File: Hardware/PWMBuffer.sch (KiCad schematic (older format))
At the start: 3 parts, among them Q2 IRLZ44N

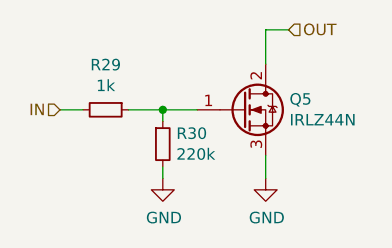
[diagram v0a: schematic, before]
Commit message: Board updates:
Fixed footprints (SMD vs. THT, no hanging pads in the air)
Added mounting holes for production
Moved F.Fab text to readable locations
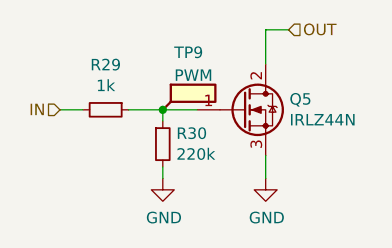
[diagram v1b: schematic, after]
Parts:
- added TP6: PWM, Measurement_Points:Measurement_Point_Round-SMD-Pad_Small, symbol Connector:TestPoint_Flag
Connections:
- net at Q2.1 (G), R23.1, R24.1: now also TP6.1
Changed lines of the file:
@@
 Wire Wire Line
 	2400 2500 2400 2550
+$Comp
+L Connector:TestPoint_Flag TP6
+U 1 1 5FA2C9EF
+P 2400 2250
+AR Path="/60041CA2/5FA2C9EF" Ref="TP6"  Part="1"
+AR Path="/60047352/5FA2C9EF" Ref="TP7"  Part="1"
+AR Path="/6005538F/5FA2C9EF" Ref="TP8"  Part="1"
+AR Path="/60055395/5FA2C9EF" Ref="TP9"  Part="1"
+F 0 "TP9" H 2450 2500 50  0000 L CNN
+F 1 "PWM" H 2450 2400 50  0000 L CNN
+F 2 "Measurement_Points:Measurement_Point_Round-SMD-Pad_Small" H 2600 2250 50  0001 C CNN
+F 3 "~" H 2600 2250 50  0001 C CNN
+	1    2400 2250
+	1    0    0    -1
+$EndComp
 $EndSCHEMATC

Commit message: Hardware v0.1, Firmware runs ADC trigger by TIM3
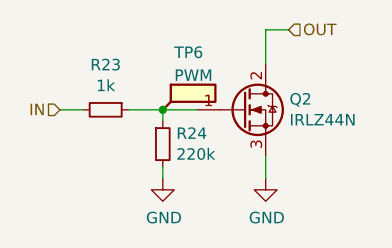
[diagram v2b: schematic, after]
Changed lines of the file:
@@
 $Descr A4 11693 8268
 encoding utf-8
-Sheet 6 6
+Sheet 3 6
 Title ""
 Date ""
@@
 AR Path="/60047352/60091104" Ref="Q3"  Part="1"
 AR Path="/60055395/60091104" Ref="Q5"  Part="1"
-F 0 "Q5" H 2954 2296 50  0000 L CNN
+F 0 "Q2" H 2954 2296 50  0000 L CNN
 F 1 "IRLZ44N" H 2954 2205 50  0000 L CNN
 F 2 "TO_SOT_Packages_THT:TO-220-3_Vertical" H 3000 2175 50  0001 L CIN
@@
 AR Path="/60047352/60093386" Ref="R25"  Part="1"
 AR Path="/60055395/60093386" Ref="R29"  Part="1"
-F 0 "R29" V 1954 2250 50  0000 C CNN
+F 0 "R23" V 1954 2250 50  0000 C CNN
 F 1 "1k" V 2045 2250 50  0000 C CNN
 F 2 "Resistors_SMD:R_0402" H 2150 2250 50  0001 C CNN
@@
 AR Path="/60047352/60093ACC" Ref="R26"  Part="1"
 AR Path="/60055395/60093ACC" Ref="R30"  Part="1"
-F 0 "R30" H 2459 2446 50  0000 L CNN
+F 0 "R24" H 2459 2446 50  0000 L CNN
 F 1 "220k" H 2459 2355 50  0000 L CNN
 F 2 "Resistors_SMD:R_0402" H 2400 2400 50  0001 C CNN
@@
 AR Path="/6005538F/5FA2C9EF" Ref="TP8"  Part="1"
 AR Path="/60055395/5FA2C9EF" Ref="TP9"  Part="1"
-F 0 "TP9" H 2450 2500 50  0000 L CNN
+F 0 "TP6" H 2450 2500 50  0000 L CNN
 F 1 "PWM" H 2450 2400 50  0000 L CNN
 F 2 "Measurement_Points:Measurement_Point_Round-SMD-Pad_Small" H 2600 2250 50  0001 C CNN
